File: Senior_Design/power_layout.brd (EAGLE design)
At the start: 108.2 x 35 mm, 105 parts, among them J1 AU-Y1008-2, J1[SIMCARD] 78646-3001, J2 U.FL-R-SMT-1(01), J3 U.FL-R-SMT-1(01), J4[GROVE] 640456-4, T1 BCX70SMD, T2 BCX70SMD, U1 SIM7000E, U2 TUSB2046BVFR, U3 MAX3373EEKA+T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

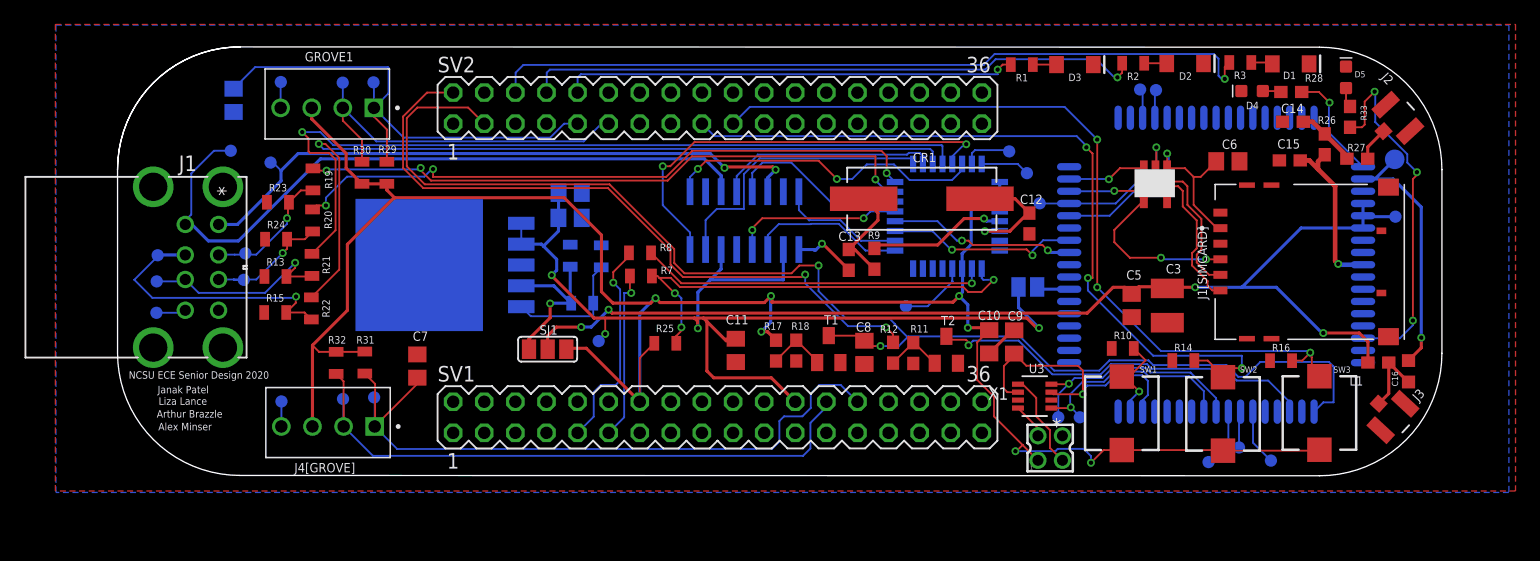
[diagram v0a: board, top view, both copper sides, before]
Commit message: Updating missing part values
Alex had assigned these before but I wrote over them on accident :)
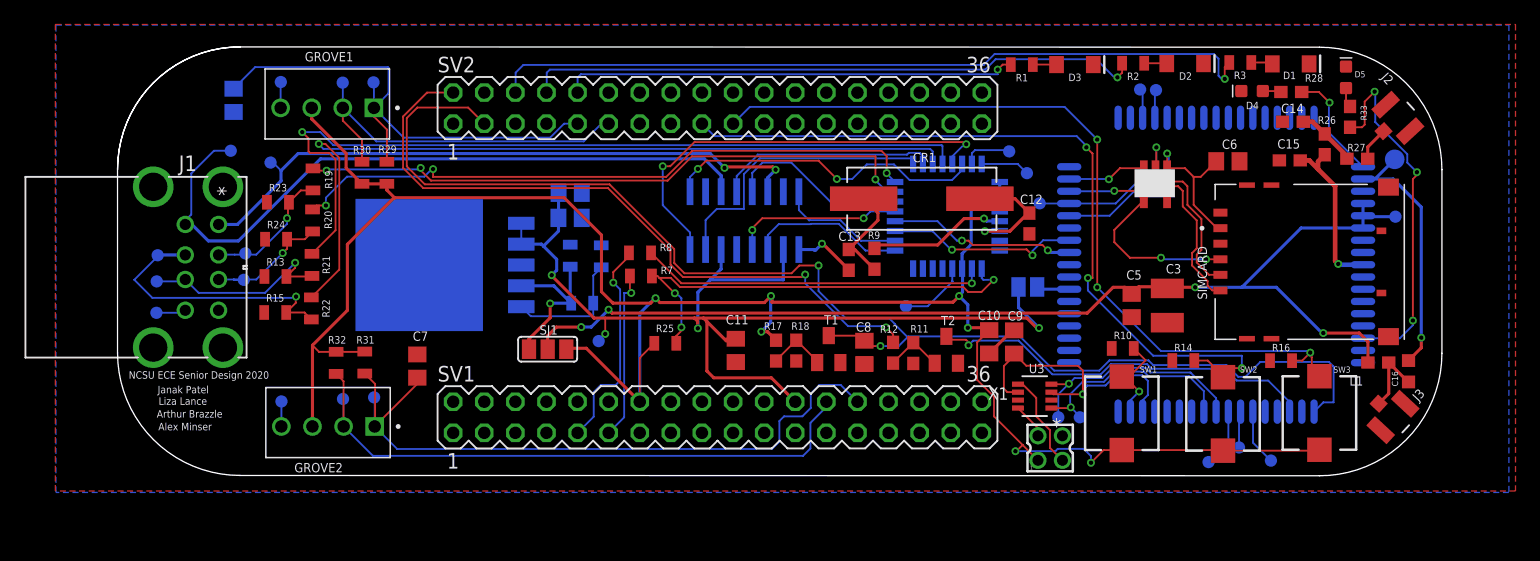
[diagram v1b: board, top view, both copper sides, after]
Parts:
- C1: value (none) -> 100uF
- C10, C11, C6, C8, C9: value (none) -> .1uF
- C4: value (none) -> 1uF
- R10, R14, R16: value (none) -> 4700
- R21, R22: value (none) -> 27
- R4: value (none) -> 47k
- R5: value (none) -> 100k
- R6: value (none) -> 470k
- renumbered J1[SIMCARD] to SIMCARD, J4[GROVE] to GROVE2, U$1 to U5

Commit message: Beta Boar Spin Files
Implemented board revisions from Alpha board.
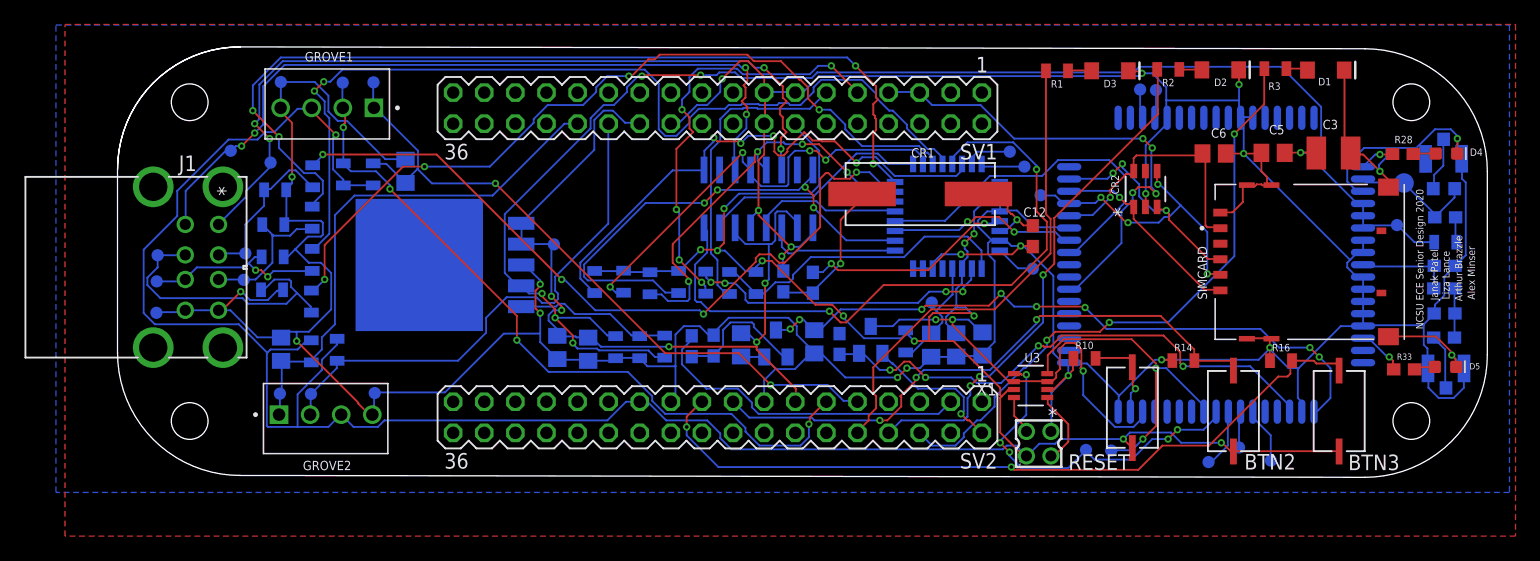
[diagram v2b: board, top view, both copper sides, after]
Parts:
- removed R12: 4.7k, SparkFun-Resistors:0603
- removed SJ1: (no value), jumper:SJ_2
- removed SJ2: (no value), jumper:SJ
- removed SW1, SW2, SW3: (no value), adafruit:PUSHBUTTON_SMD_SJ
- removed U5: MSQA6V1W5T2G, Personal:SOT-23-5_M5
- added BTN2, BTN3, RESET: PTS636SM25F, Personal:SW2_PTS636_SM25F_SMTR_LFS_CNK
- added C17: 3uF, rcl:C0805
- added CR2: ESDA6V1-5SC6SOT23-6L_STM-M, Personal:SOT23-6L_STM-M
- added R34, R35, R36, R37: 15k, SparkFun-Resistors:0805
- added R38: 45k, SparkFun-Resistors:0805
- added R39: 10, SparkFun-Resistors:0805
- added TP20: TPTP10R, testpad:TP10R
- moved SV1 25.2 mm to (49.0, 30.0), turned to 180 degrees
- moved SV2 25.2 mm to (49.0, 4.75), turned to 180 degrees
- moved D5 25.0 mm to (108.5, 8.86), turned to 0 degrees
- moved J3 21.5 mm to (108.3, 25.9), flipped to the bottom, turned to 179.8 degrees
- moved R33 21.1 mm to (105.1, 8.66), turned to 180 degrees
- moved J2 20.8 mm to (108.5, 8.74), flipped to the bottom, turned to 0.1 degrees
- moved C14 20.0 mm to (108.4, 13.2), flipped to the bottom, turned to 0 degrees
- moved C3 18.4 mm to (99.3, 26.3), turned to 0 degrees
- moved C5 17.0 mm to (94.4, 26.3), turned to 180 degrees
- moved D4 16.7 mm to (108.5, 26.3), turned to 0 degrees
- moved R27 16.2 mm to (108.3, 11.3), flipped to the bottom
- moved C15 15.3 mm to (108.4, 17.1), flipped to the bottom
- moved R26 15.3 mm to (108.3, 15.3), flipped to the bottom, turned to 0 degrees
- moved C16 15.2 mm to (108.3, 23.4), flipped to the bottom, turned to 180 degrees
- moved C2 15.2 mm to (23.5, 24.8), turned to 270 degrees
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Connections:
- removed net +5V: C1.1, C11.1, C4.1, POWER_SUPPLY.1, POWER_SUPPLY.2, SJ2.1, SV1.24, TP6.TP, U4.2, U4.6
- removed net MODEM_POWER: C3.1, C5.1, L1.1, SJ1.2, TP5.TP, U1.55, U1.56, U1.57
- removed net N$16 (its old number): U3.5, X1.3
- removed net N$17: R11.1, R12.2, T2.1
- removed net VDD_EXT: T2.3, U1.3
- new net 0: R11.1
- new net 5V: C1.1, C11.1, C4.1, POWER_SUPPLY.1, POWER_SUPPLY.2, SV1.24, SV2.13, TP6.TP, U4.2, U4.6
- new net N$23: C8.1, T1.3, U1.1
- new net N$38: U3.1, X1.3
- new net RXD: TP16.TP, U1.10, U3.4
- new net TXD: TP15.TP, U1.9, U3.5
- new net USB_VBUS: SV1.5, SV1.7, U1.24
- net 1.8V: now also T2.3
- net 3.3V: now also BTN2.1, BTN3.1, R34.2, R35.2, R36.1, R37.1, R38.1, RESET.1, SV2.23, U3.7; no longer R17.2, SJ1.1, SW1.P$2, SW2.P$2, SW3.P$2
- net GND: now also C17.2, CR2.2, SV1.13, SV1.16, SV1.22, SV2.21; no longer R11.2, T2.2, U3.7, U5.P$2
- net N$1: now also CR2.6; no longer U5.P$5
- net N$15: no longer L1.2
- net N$2: now also CR2.3, SIMCARD.C2; no longer SIMCARD.C3, U5.P$3
- net N$27: now also L1.1, R39.1; no longer TP16.TP, U1.10, U3.1
- net N$28: now also TP20.TP, U2.32; no longer TP15.TP, U1.9, U3.4
- net N$34: now also C17.1, R38.2
- net N$36: now also R11.2, T2.2, U1.3; no longer SJ2.2, U1.24
- net N$4: now also CR2.1, SIMCARD.C3; no longer SIMCARD.C2, U5.P$1
- net N$6: now also CR2.4; no longer U5.P$4
- net NRESET: now also RESET.2; no longer SW1.P$1
- net OVRCUR1: now also R35.1
- net OVRCUR2: now also R34.1
- net OVRCUR3: now also R37.2
- net OVRCUR4: now also R36.2
- net PB2: now also BTN2.2; no longer SW2.P$1
- net PB3: now also BTN3.2; no longer SW3.P$1
- net PRE_GPS: now also L1.2
- net PWRKEY: now also R17.2; no longer C8.1, T1.3, U1.1
- net REGULATED: now also C3.1, C5.1, R39.2, TP5.TP, U1.55, U1.56, U1.57; no longer SJ1.3
- net SLEEP: now also T2.1; no longer R12.1
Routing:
- net GND: track 14.9 -> 448.3 mm, vias 1 -> 23
- net REGULATED: track 13.9 -> 123.5 mm, vias 1 -> 6
- net +5V: track 91.7 -> 0.00 mm, vias 4 -> 0
- net MODEM_POWER: track 90.6 -> 0.00 mm, vias 4 -> 0
- net PWRKEY: track 109.7 -> 26.9 mm, vias 2 -> 0
- net 3.3V: track 174.2 -> 248.5 mm, vias 7 -> 12
- net 5V: track 0.00 -> 70.9 mm, vias 0 -> 5
- net N$23: track 0.00 -> 54.0 mm, vias 0 -> 8
- net SLEEP: track 56.8 -> 12.0 mm, vias 2 -> 1
- net N$36: track 2.69 -> 43.5 mm, vias 0 -> 4
- net USB_VBUS: track 0.00 -> 40.0 mm, vias 0 -> 4
- net VDD_EXT: track 32.2 -> 0.00 mm, vias 1 -> 0
- net OVRCUR1: track 10.4 -> 41.4 mm, vias 0 -> 4
- net I2C1_SDA: track 30.6 -> 59.9 mm, vias 0 -> 4
- net TXD: track 0.00 -> 29.1 mm, vias 0 -> 5
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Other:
- board size 108.2 x 35 mm -> 111.9 x 35.2 mm

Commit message: Add files via upload
This push includes the changes from Dr Pitts' Review and is THE Beta Board for purchasing.
-Cam files are processed in the folder "Beta Spin"
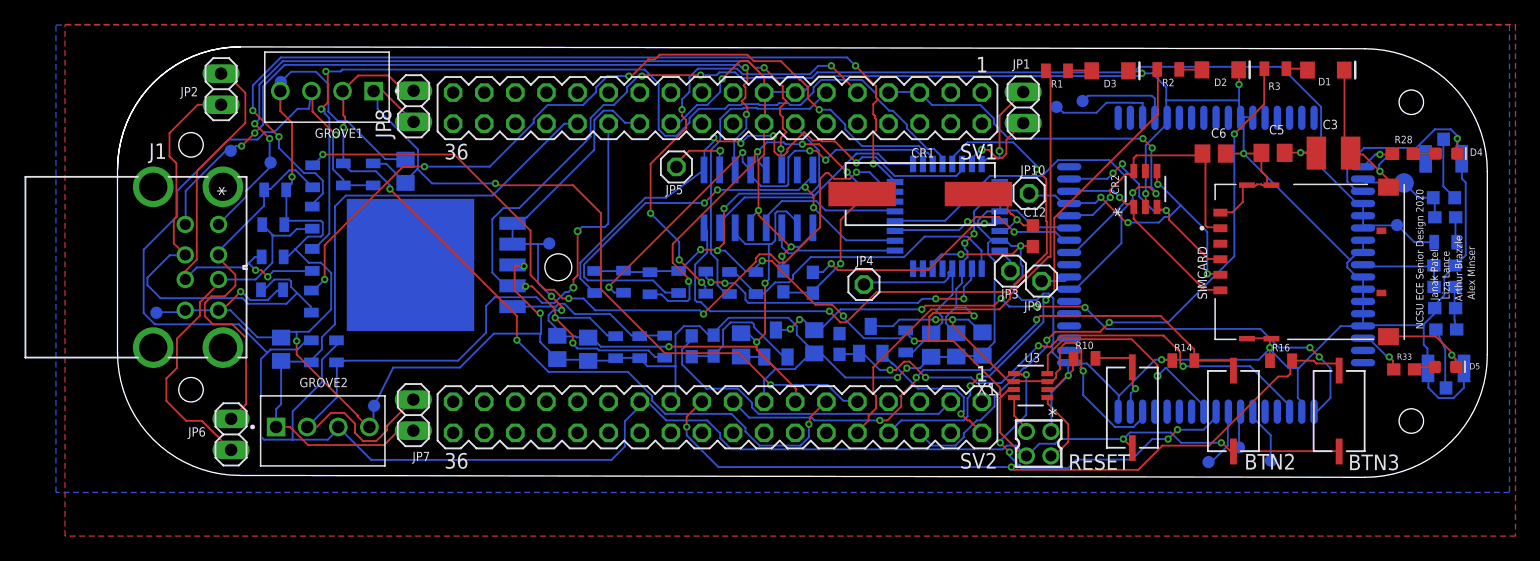
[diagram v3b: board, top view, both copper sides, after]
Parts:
- removed TP10, TP11, TP12, TP13, TP14, TP15, TP16, TP17, TP18, TP19, TP20, TP23, TP24, TP25, TP9: TPTP10R, testpad:TP10R
- added JP1, JP2, JP6, JP7, JP8: (no value), pinhead:1X02
- added JP10, JP3, JP4, JP5, JP9: (no value), pinhead:1X01
- moved TP7 69.5 mm to (78.8, 30.6)
- moved TP8 67.9 mm to (76.7, 30.1)
- moved GROVE1 1.37 mm to (20.9, 31.4)
- moved TP26 1.04 mm to (21.0, 5.69)
- moved GROVE2 1.04 mm to (12.9, 3.96)
- moved C16 0.74 mm to (108.3, 22.7), turned to 0 degrees
- moved POWER_SUPPLY 0.71 mm to (26.5, 17.2)
- moved R27 0.68 mm to (108.5, 11.9)
- moved C14 0.43 mm to (108.4, 13.7)
- moved TP6 0.39 mm to (35.3, 18.9)
- moved R32 0.14 mm to (17.9, 10.1)
- moved R26 0.13 mm to (108.4, 15.4)
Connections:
- removed net N$24: TP17.TP, U1.38
- removed net N$25: TP23.TP, U2.24
- removed net N$26: TP24.TP, U2.23
- removed net N$28: TP20.TP, U2.32
- removed net N$31: TP18.TP, U1.37
- removed net N$34: C17.1, R38.2, TP25.TP, U2.4
- removed net N$6: CR2.4, SIMCARD.C7, TP19.TP, U1.31
- new net DM4: JP1.1, U2.23
- new net DP4: JP1.2, U2.24
- new net RESET: C17.1, JP4.1, R38.2, U2.4
- new net SIMC_ADC: JP9.1, U1.25
- new net SIMC_I2C_SCL: TP7.TP, U1.38
- new net SIMC_I2C_SDA: TP8.TP, U1.37
- new net SIM_DATA: CR2.4, JP10.1, SIMCARD.C7, U1.31
- new net SUSPEND: JP3.1, U2.32
- net I2C1_SCL: now also JP8.1; no longer TP11.TP
- net I2C1_SDA: now also JP8.2; no longer TP12.TP
- net I2C2_SCL: now also JP7.1; no longer TP13.TP
- net I2C2_SDA: now also JP7.2; no longer TP14.TP
- net OUT4: now also JP5.1
- net RXD: no longer TP16.TP
- net TXD: no longer TP15.TP
- net USB1_D+: now also JP6.2; no longer TP8.TP
- net USB1_D-: now also JP6.1; no longer TP7.TP
- net USB2_D+: now also JP2.2; no longer TP10.TP
- net USB2_D-: now also JP2.1; no longer TP9.TP
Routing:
- net SIM_DATA: track 0.00 -> 25.7 mm, vias 0 -> 4
- net N$6: track 24.7 -> 0.00 mm, vias 4 -> 0
- net USB1_D+: track 11.9 -> 30.5 mm
- net USB2_D+: track 15.3 -> 32.8 mm
- net USB1_D-: track 13.3 -> 30.5 mm
- net RESET: track 0.00 -> 17.2 mm
- net USB2_D-: track 24.4 -> 39.6 mm
- net I2C2_SDA: track 42.8 -> 57.6 mm, vias 0 -> 2
- net I2C2_SCL: track 42.8 -> 56.6 mm
- net N$34: track 10.0 -> 0.00 mm
- net SIMC_I2C_SDA: track 0.00 -> 8.79 mm
- net 3.3V: track 248.5 -> 257.2 mm
- net RXD: track 27.0 -> 18.6 mm, vias 2 -> 1
- net DP4: track 0.00 -> 7.91 mm, vias 0 -> 1
- net GND: track 448.3 -> 456.2 mm
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
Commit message: Adding Final Design Files
Incorporated all changes from Beta Assembly
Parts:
- removed TP27, TP28: TPTP10R, testpad:TP10R
- R6: value 470k -> 1500
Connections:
- net 0: now also RESET.2
- net 3.3V: now also R10.2; no longer RESET.1
- net GND: no longer R10.1, TP27.TP, TP28.TP
- net NRESET: now also R10.1, RESET.1; no longer R10.2, RESET.2
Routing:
- net GND: track 456.2 -> 532.3 mm, vias 23 -> 8
- net 3.3V: track 257.2 -> 220.2 mm, vias 12 -> 5
- net OVRCUR3: track 37.4 -> 68.7 mm, vias 4 -> 2
- net N$23: track 53.7 -> 84.8 mm, vias 8 -> 0
- net 0: track 0.00 -> 27.1 mm, vias 0 -> 3
- net N$16: track 65.6 -> 91.9 mm, vias 4 -> 2
- net OVRCUR2: track 34.3 -> 59.8 mm, vias 4 -> 2
- net NRESET: track 7.54 -> 30.7 mm, vias 1 -> 2
- net I2C2_SDA: track 57.6 -> 42.8 mm, vias 2 -> 0
- net USB2_D-: track 39.6 -> 25.3 mm
- net MODEM_D+: track 29.9 -> 17.7 mm
- net I2C1_SDA: track 66.0 -> 78.2 mm, vias 4 -> 1
- net LED2: track 42.3 -> 54.3 mm
- net N$19: track 64.4 -> 53.1 mm, vias 4 -> 2
- net DM0: track 36.6 -> 25.4 mm, vias 5 -> 3
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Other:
- board text added: "Liza Chevalier"
- board text removed: "Liza Lance"
